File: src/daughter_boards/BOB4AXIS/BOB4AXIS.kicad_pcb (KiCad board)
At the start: 2 copper layers, 100 x 93 mm, 45 parts, among them J1 Screw_Terminal_01x03, J2 Screw_Terminal_01x03, J3 Screw_Terminal_01x03, J4 Screw_Terminal_01x03, J5 Screw_Terminal_01x08, J6 Screw_Terminal_01x08, J7 Screw_Terminal_01x08, J8 Screw_Terminal_01x08, J9 Conn_02x13_Odd_Even, U1 LTV-814, U2 LTV-814, U3 LTV-814, U4 LTV-814, U5 AM26LS31CD, U6 AM26LS31CD, U7 KF142V-5_08-2P, U8 74HC86, U9 AM26LS31CD

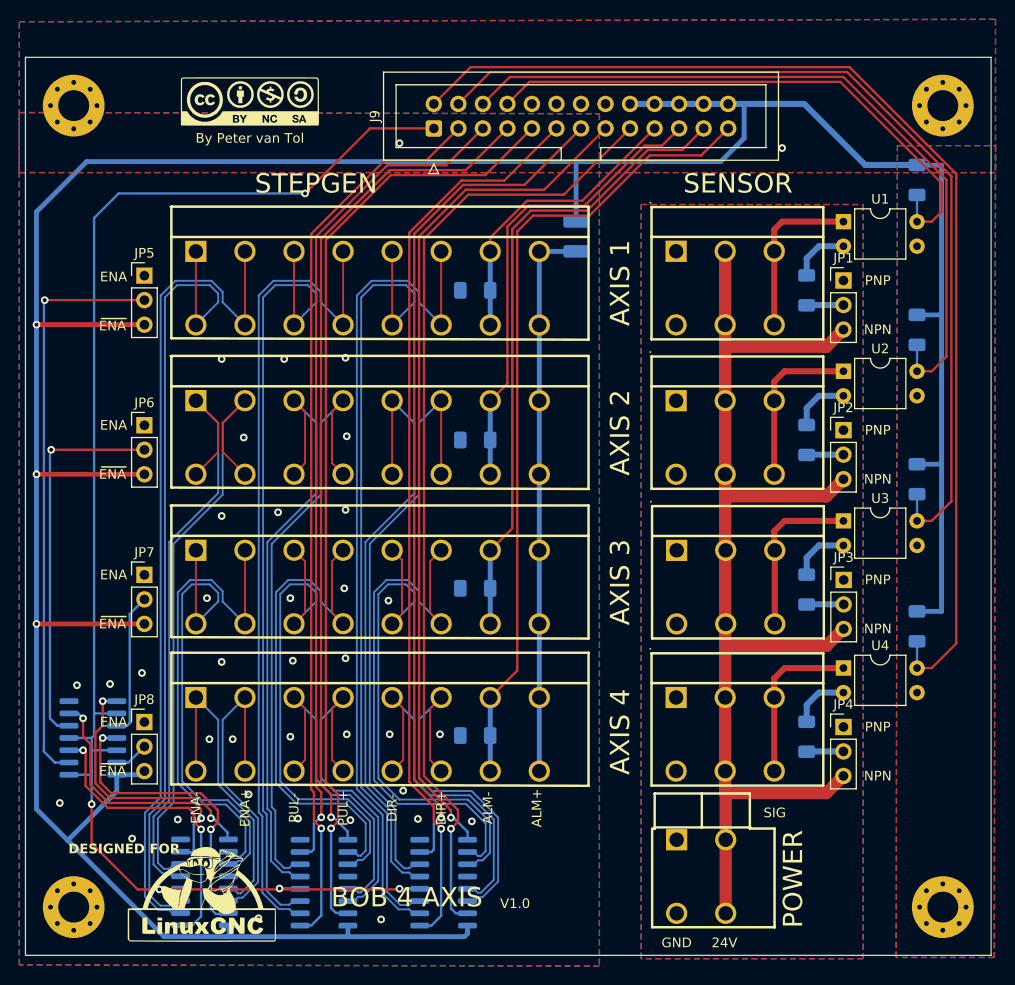
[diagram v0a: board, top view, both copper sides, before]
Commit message: Decoupling capacitors
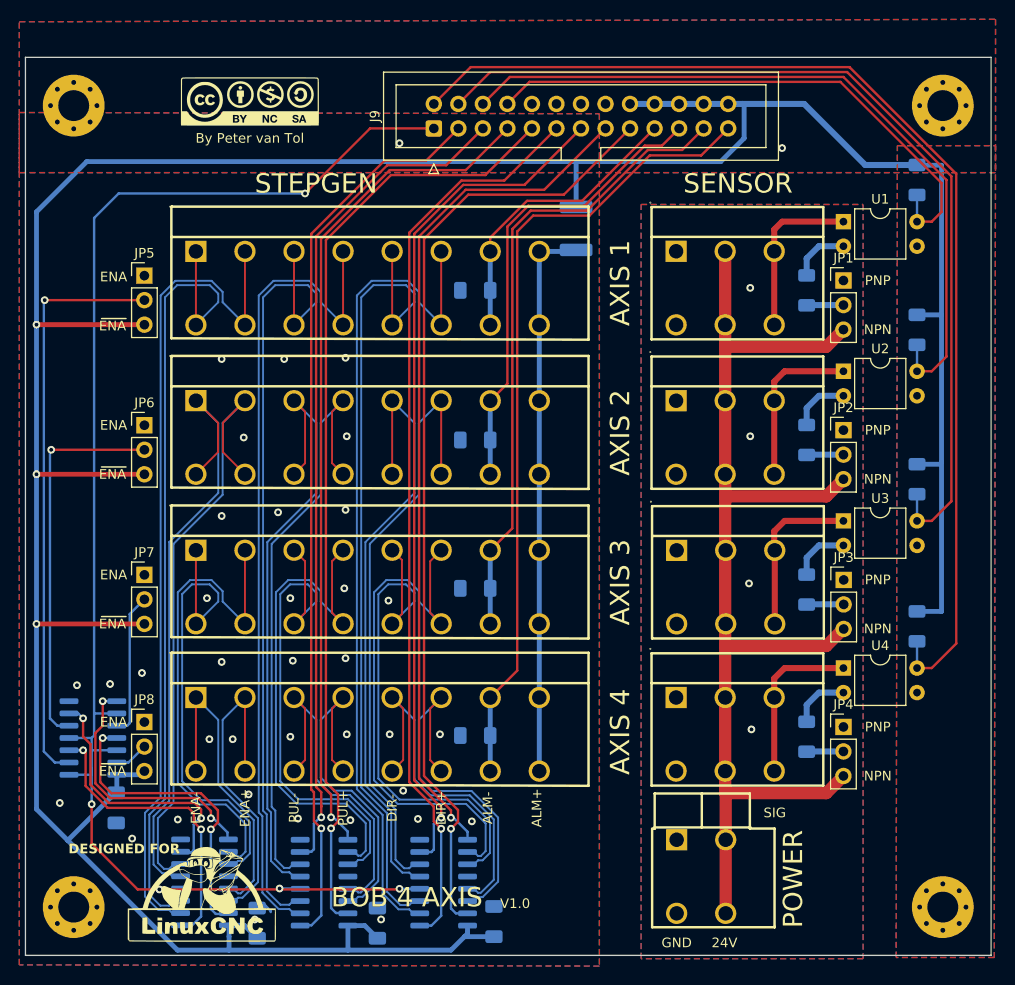
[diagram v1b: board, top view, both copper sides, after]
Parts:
- added C1: 0.1uF, Capacitor_SMD:C_1206_3216Metric_Pad1.33x1.80mm_HandSolder, B.Cu at (48.5, 89.5)
- added C2: 0.1uF, Capacitor_SMD:C_1206_3216Metric_Pad1.33x1.80mm_HandSolder, B.Cu at (9.40, 77.7)
- added C3: 0.1uF, Capacitor_SMD:C_1206_3216Metric_Pad1.33x1.80mm_HandSolder, B.Cu at (24.0, 89.7)
- added C4: 0.1uF, Capacitor_SMD:C_1206_3216Metric_Pad1.33x1.80mm_HandSolder, B.Cu at (36.4, 89.7)
- F1: footprint Resistor_SMD:R_1210_3225Metric_Pad1.30x2.65mm_HandSolder -> Resistor_SMD:R_1812_4532Metric_Pad1.30x3.40mm_HandSolder
- moved F1 0.82 mm to (57.0, 17.7)
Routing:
- net +5V: track 335.8 -> 348.6 mm
- net GND: track 0.00 -> 2.02 mm
- net GND1: vias 0 -> 4
